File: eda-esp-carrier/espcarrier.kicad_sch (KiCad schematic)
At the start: 42 parts, among them J1 B-, J2 B+, J3 DEBUG, Q1 PMF170XP, U1 TP4056_board, U2 ESP-12E, U3 TLV75533PDBV

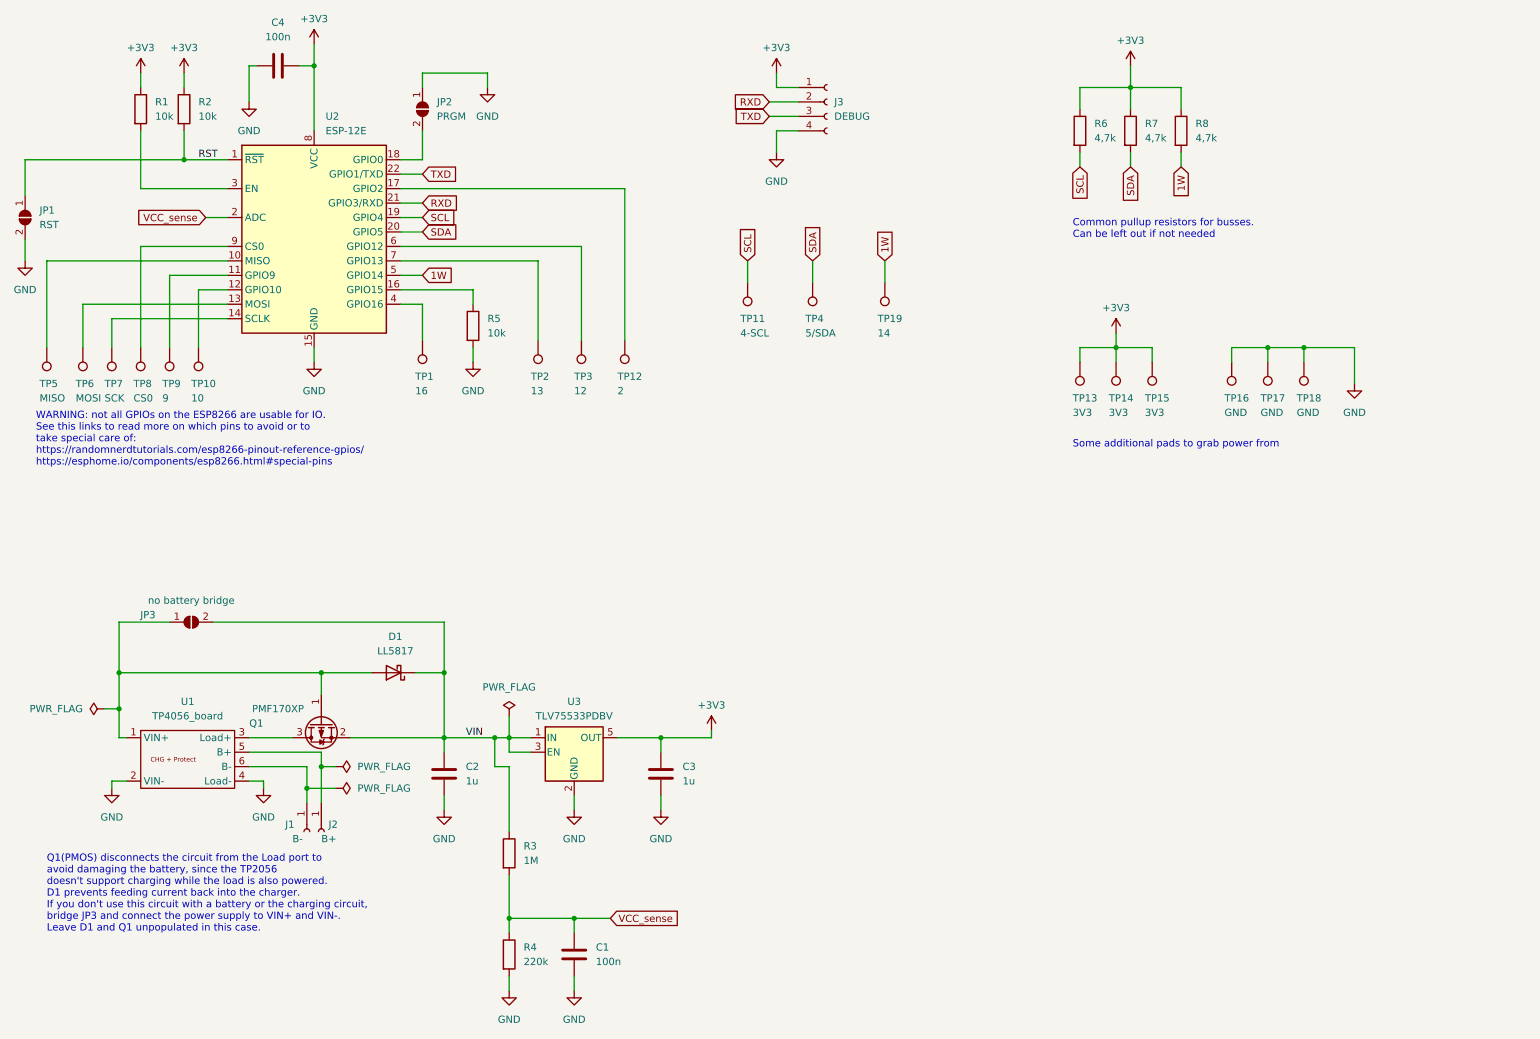
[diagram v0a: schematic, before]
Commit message: Complete redo: * make board bigger to fit sensor case * Add simple breakout to just breakout all GPIOs * Add carrier board which stacks on daughterboards * Add templates and library items for creating custom   daughterboards easily * begin working on docs for these boards * add dxf drawings for all relevant parts
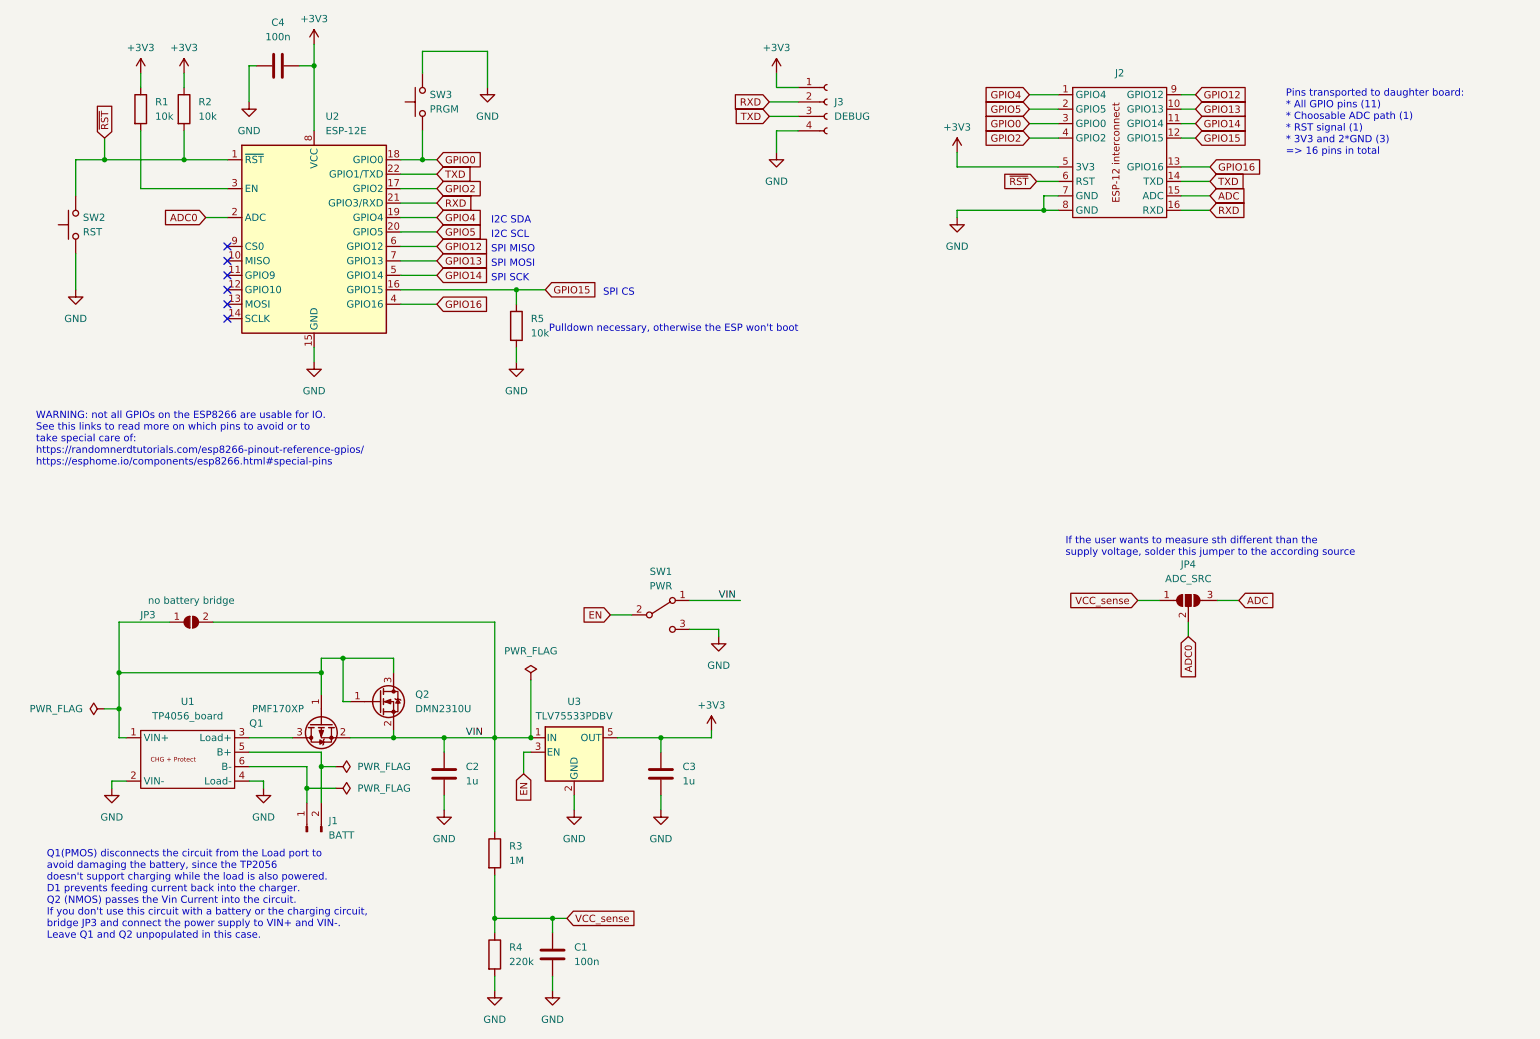
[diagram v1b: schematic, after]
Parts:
- removed D1: LL5817, Diode_SMD:D_SOD-123, symbol Device:D_Schottky
- removed J1: B-, TestPoint:TestPoint_Pad_3.0x3.0mm, symbol Connector:Conn_01x01_Socket
- removed J2: B+, TestPoint:TestPoint_Pad_3.0x3.0mm, symbol Connector:Conn_01x01_Socket
- removed JP1: RST, Jumper:SolderJumper-2_P1.3mm_Open_RoundedPad1.0x1.5mm, symbol Jumper:SolderJumper_2_Open
- removed JP2: PRGM, Jumper:SolderJumper-2_P1.3mm_Open_RoundedPad1.0x1.5mm, symbol Jumper:SolderJumper_2_Open
- removed R6, R7, R8: 4,7k, Resistor_SMD:R_0805_2012Metric_Pad1.20x1.40mm_HandSolder, symbol Device:R
- removed TP1: 16, TestPoint:TestPoint_Pad_1.5x1.5mm, symbol Connector:TestPoint
- removed TP10: 10, TestPoint:TestPoint_Pad_1.5x1.5mm, symbol Connector:TestPoint
- removed TP11: 4-SCL, TestPoint:TestPoint_Pad_1.5x1.5mm, symbol Connector:TestPoint
- removed TP12: 2, TestPoint:TestPoint_Pad_1.5x1.5mm, symbol Connector:TestPoint
- removed TP13, TP14, TP15: 3V3, TestPoint:TestPoint_Pad_1.5x1.5mm, symbol Connector:TestPoint
- removed TP16, TP17, TP18: GND, TestPoint:TestPoint_Pad_1.5x1.5mm, symbol Connector:TestPoint
- removed TP19: 14, TestPoint:TestPoint_Pad_1.5x1.5mm, symbol Connector:TestPoint
- removed TP2: 13, TestPoint:TestPoint_Pad_1.5x1.5mm, symbol Connector:TestPoint
- removed TP3: 12, TestPoint:TestPoint_Pad_1.5x1.5mm, symbol Connector:TestPoint
- removed TP4: 5/SDA, TestPoint:TestPoint_Pad_1.5x1.5mm, symbol Connector:TestPoint
- removed TP5: MISO, TestPoint:TestPoint_Pad_1.5x1.5mm, symbol Connector:TestPoint
- removed TP6: MOSI, TestPoint:TestPoint_Pad_1.5x1.5mm, symbol Connector:TestPoint
- removed TP7: SCK, TestPoint:TestPoint_Pad_1.5x1.5mm, symbol Connector:TestPoint
- removed TP8: CS0, TestPoint:TestPoint_Pad_1.5x1.5mm, symbol Connector:TestPoint
- removed TP9: 9, TestPoint:TestPoint_Pad_1.5x1.5mm, symbol Connector:TestPoint
- added J1: BATT, Connector_PinHeader_2.54mm:PinHeader_2x01_P2.54mm_Vertical, symbol Connector:Conn_01x02_Pin
- added J2: ~, esp-board-lib:carrier-template, symbol esp-board-lib:ESP12-breakout-interconnect
- added JP4: ADC_SRC, Jumper:SolderJumper-3_P1.3mm_Open_RoundedPad1.0x1.5mm_NumberLabels, symbol Jumper:SolderJumper_3_Open
- added Q2: DMN2310U, Package_TO_SOT_SMD:SOT-23-3, symbol Device:Q_NMOS_GSD
- added SW1: PWR, Button_Switch_SMD:SW_SPDT_PCM12, symbol Switch:SW_SPDT
- added SW2: RST, Button_Switch_SMD:SW_Tactile_SPST_NO_Straight_CK_PTS636Sx25SMTRLFS, symbol Switch:SW_Push
- added SW3: PRGM, Button_Switch_SMD:SW_Tactile_SPST_NO_Straight_CK_PTS636Sx25SMTRLFS, symbol Switch:SW_Push
- U1: footprint anphi:TP4056-18650 -> anphi_util:TP4056-18650; symbol anphi:TP4056_board -> anphi_util:TP4056_board
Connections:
- net +3V3: now also J2.5 (3V3)
- net GND: now also J2.7 (GND), J2.8 (GND), SW1.3 (C), SW2.1, SW3.2
- net RXD: now also J2.16 (RXD)
- net TXD: now also J2.14 (TXD)
- net VCC_sense: now also JP4.1 (A); no longer U2.2 (ADC)
- net VIN: now also Q2.2 (S), SW1.1 (A); no longer U3.3 (EN)
- net at JP3.1 (A), Q1.1 (G), U1.1 (VIN+): now also Q2.1 (G), Q2.3 (D)
- net GPIO15: now reaches R5.1, U2.16 (GPIO15)
- net GPIO15: now also J2.12 (GPIO15)
- net GPIO2: now reaches U2.17 (GPIO2)
- net GPIO2: now also J2.4 (GPIO2)
- net GPIO0: now reaches U2.18 (GPIO0)
- net GPIO0: now also J2.3 (GPIO0), SW3.1
- net GPIO16: now reaches U2.4 (GPIO16)
- net GPIO16: now also J2.13 (GPIO16)
- net GPIO12: now reaches U2.6 (GPIO12)
- net GPIO12: now also J2.9 (GPIO12)
- net GPIO13: now reaches U2.7 (GPIO13)
- net GPIO13: now also J2.10 (GPIO13)
- net at U1.6 (B-): now also J1.1 (Pin_1)
- net at U1.5 (B+): now also J1.2 (Pin_2)
- net 1W renamed GPIO14
- net GPIO14: now also J2.11 (GPIO14)
- net RST renamed ~{RST}
- net ~{RST}: now also J2.6 (RST), SW2.2
- net SCL renamed GPIO4
- net GPIO4: now also J2.1 (GPIO4)
- net SDA renamed GPIO5
- net GPIO5: now also J2.2 (GPIO5)
- new net ADC: J2.15 (ADC), JP4.3 (B)
- new net ADC0: JP4.2 (C), U2.2 (ADC)
- new net EN: SW1.2 (B), U3.3 (EN)
- no-connect marks 0 -> 6
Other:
- note added: "I2C SCL"
- note added: "I2C SDA"
- note added: "If the user wants to measure sth different than the supply voltage, solder this jumper to the according source"
- note added: "Pins transported to daughter board: * All GPIO pins (11) * Choosable ADC path (1) * RST signal (1) * 3V3 and 2*GND (3) => 16 pins in total"
- note added: "Pulldown necessary, otherwise the ESP won't boot"
- note added: "Q1(PMOS) disconnects the circuit from the Load port to avoid damaging the battery, since the TP2056 doesn't support charging while the load is also powered. D1 prevents feeding current back into the charger. Q2 (NMOS) passes the Vin Current into the circuit. If you don't use this circuit with a battery or the charging circuit, bridge JP3 and connect the power supply to VIN+ and VIN-. Leave Q1 and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"
- note added: "SPI CS"
- note added: "SPI MISO"
- note added: "SPI MOSI"
- note added: "SPI SCK"
- note removed: "Common pullup resistors for busses. Can be left out if not needed"
- note removed: "Q1(PMOS) disconnects the circuit from the Load port to avoid damaging the battery, since the TP2056 doesn't support charging while the load is also powered. D1 prevents feeding current back into the charger. If you don't use this circuit with a battery or the charging circuit, bridge JP3 and connect the power supply to VIN+ and VIN-. Leave D1 and Q1 unpopulated in this case."
- note removed: "Some additional pads to grab power from"
- moved on the sheet: C1, R3, R4, R5

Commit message: finish rf friendlier desgin
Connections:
- net B+: now reaches J1.2 (Pin_2), U1.5 (B+)
- net B-: now reaches J1.1 (Pin_1), U1.6 (B-)
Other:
- moved on the sheet: JP4
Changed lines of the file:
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@@
   (junction (at 97.79 173.99) (diameter 0) (color 0 0 0 0)
+  )
+  (junction (at 74.93 121.92) (diameter 0) (color 0 0 0 0)
   )
   (junction (at 43.18 40.64) (diameter 0) (color 0 0 0 0)
@@
     (stroke (width 0) (type default))
   )
+  (wire (pts (xy 74.93 121.92) (xy 48.26 121.92))
+    (stroke (width 0) (type default))
+  )
   (wire (pts (xy 119.38 142.24) (xy 127 142.24))
     (stroke (width 0) (type default))
@@
     (stroke (width 0) (type default))
   )
-  (wire (pts (xy 97.79 121.92) (xy 48.26 121.92))
+  (wire (pts (xy 97.79 121.92) (xy 74.93 121.92))
     (stroke (width 0) (type default))
   )
@@
     (stroke (width 0) (type default))
   )
+  (wire (pts (xy 74.93 115.57) (xy 74.93 121.92))
+    (stroke (width 0) (type default))
+  )
   (wire (pts (xy 97.79 121.92) (xy 97.79 142.24))
     (stroke (width 0) (type default))
@@
     (stroke (width 0) (type default))
   )
-  (wire (pts (xy 224.79 118.11) (xy 228.6 118.11))
+  (wire (pts (xy 236.22 82.55) (xy 240.03 82.55))
     (stroke (width 0) (type default))
   )
@@
     (stroke (width 0) (type default))
   )
-  (wire (pts (xy 214.63 118.11) (xy 210.82 118.11))
-    (stroke (width 0) (type default))
-  )
-  (wire (pts (xy 219.71 121.92) (xy 219.71 124.46))
+  (wire (pts (xy 226.06 82.55) (xy 222.25 82.55))
+    (stroke (width 0) (type default))
+  )
+  (wire (pts (xy 231.14 86.36) (xy 231.14 88.9))
     (stroke (width 0) (type default))
   )
@@
   )
   (text "If the user wants to measure sth different than the\nsupply voltage, solder this jumper to the according source"
-    (at 198.12 110.49 0)
+    (at 209.55 74.93 0)
     (effects (font (size 1.27 1.27)) (justify left bottom))
   )
@@
     (effects (font (size 1.27 1.27)) (justify left bottom))
   )
-  (label "VIN" (at 92.71 142.24 0) (fields_autoplaced)
+  (label "B+" (at 57.15 144.78 0) (fields_autoplaced)
+    (effects (font (size 1.27 1.27)) (justify left bottom))
+  )
+  (label "B-" (at 57.15 147.32 0) (fields_autoplaced)
     (effects (font (size 1.27 1.27)) (justify left bottom))
   )
@@
     )
   )
-  (global_label "VCC_sense" (shape input) (at 210.82 118.11 180) (fields_autoplaced)
+  (global_label "VCC_sense" (shape input) (at 222.25 82.55 180) (fields_autoplaced)
     (effects (font (size 1.27 1.27)) (justify right))
-    (property "Intersheetrefs" "${INTERSHEET_REFS}" (at 198.4283 118.0306 0)
+    (property "Intersheetrefs" "${INTERSHEET_REFS}" (at 209.8583 82.4706 0)
       (effects (font (size 1.27 1.27)) (justify right) hide)
     )
@@
     )
   )
+  (global_label "VIN" (shape input) (at 74.93 115.57 90) (fields_autoplaced)
+    (effects (font (size 1.27 1.27)) (justify left))
+    (property "Intersheetrefs" "${INTERSHEET_REFS}" (at 74.93 109.5609 90)
+      (effects (font (size 1.27 1.27)) (justify left) hide)
+    )
+  )
   (global_label "GPIO0" (shape input) (at 87.63 40.64 0) (fields_autoplaced)
     (effects (font (size 1.27 1.27)) (justify left))
@@
     )
   )
-  (global_label "ADC" (shape input) (at 228.6 118.11 0) (fields_autoplaced)
-    (effects (font (size 1.27 1.27)) (justify left))
-    (property "Intersheetrefs" "${INTERSHEET_REFS}" (at 235.2138 118.11 0)
+  (global_label "ADC" (shape input) (at 240.03 82.55 0) (fields_autoplaced)
+    (effects (font (size 1.27 1.27)) (justify left))
+    (property "Intersheetrefs" "${INTERSHEET_REFS}" (at 246.6438 82.55 0)
       (effects (font (size 1.27 1.27)) (justify left) hide)
     )
@@
     )
   )
-  (global_label "ADC0" (shape input) (at 219.71 124.46 270) (fields_autoplaced)
+  (global_label "ADC0" (shape input) (at 231.14 88.9 270) (fields_autoplaced)
     (effects (font (size 1.27 1.27)) (justify right))
-    (property "Intersheetrefs" "${INTERSHEET_REFS}" (at 219.71 132.2833 90)
+    (property "Intersheetrefs" "${INTERSHEET_REFS}" (at 231.14 96.7233 90)
       (effects (font (size 1.27 1.27)) (justify right) hide)
     )
@@
     )
   )
-  (symbol (lib_id "Jumper:SolderJumper_3_Open") (at 219.71 118.11 0) (unit 1)
-    (in_bom yes) (on_board yes) (dnp no) (fields_autoplaced)
-    (property "Reference" "JP4" (at 219.71 111.76 0)
-      (effects (font (size 1.27 1.27)))
-    )
-    (property "Value" "ADC_SRC" (at 219.71 114.3 0)
-      (effects (font (size 1.27 1.27)))
-    )
-    (property "Footprint" "Jumper:SolderJumper-3_P1.3mm_Open_RoundedPad1.0x1.5mm_NumberLabels" (at 219.71 118.11 0)
-      (effects (font (size 1.27 1.27)) hide)
-    )
-    (property "Datasheet" "~" (at 219.71 118.11 0)
-      (effects (font (size 1.27 1.27)) hide)
-    )
+  (symbol (lib_id "Jumper:SolderJumper_3_Open") (at 231.14 82.55 0) (unit 1)
+    (in_bom yes) (on_board yes) (dnp no) (fields_autoplaced)
+    (property "Reference" "JP4" (at 231.14 76.2 0)
+      (effects (font (size 1.27 1.27)))
+    )
+    (property "Value" "ADC_SRC" (at 231.14 78.74 0)
+      (effects (font (size 1.27 1.27)))
+    )
+    (property "Footprint" "Jumper:SolderJumper-3_P1.3mm_Open_RoundedPad1.0x1.5mm_NumberLabels" (at 231.14 82.55 0)
+      (effects (font (size 1.27 1.27)) hide)
+    )
+    (property "Datasheet" "~" (at 231.14 82.55 0)
+      (effects (font (size 1.27 1.27)) hide)
+    )
